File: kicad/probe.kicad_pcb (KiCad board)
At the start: 2 copper layers, 36.2 x 36.2 mm, 5 parts, among them J1 Conn_01x11, J2 Conn_01x11, J3 Conn_01x11, J4 Conn_01x11, U1 QFN44

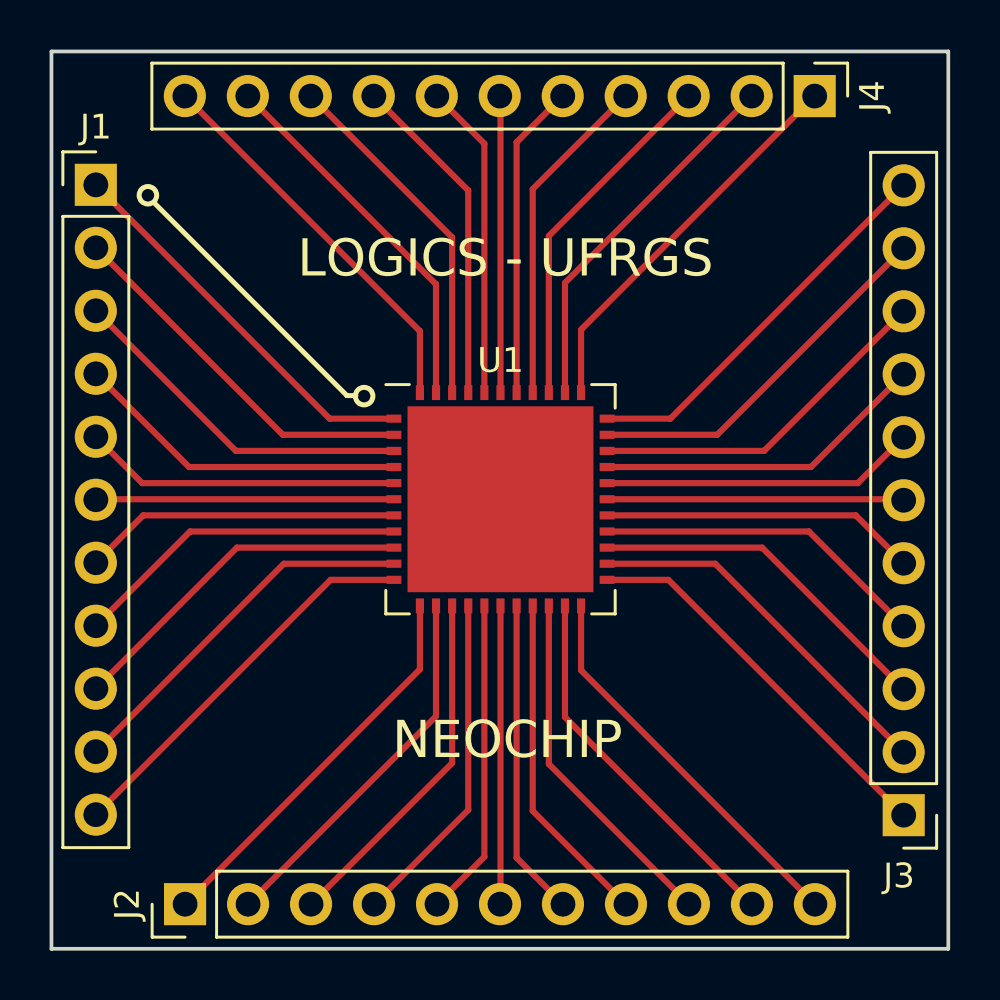
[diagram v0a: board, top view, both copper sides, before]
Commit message: LAYOUT: Modified U1 footprint
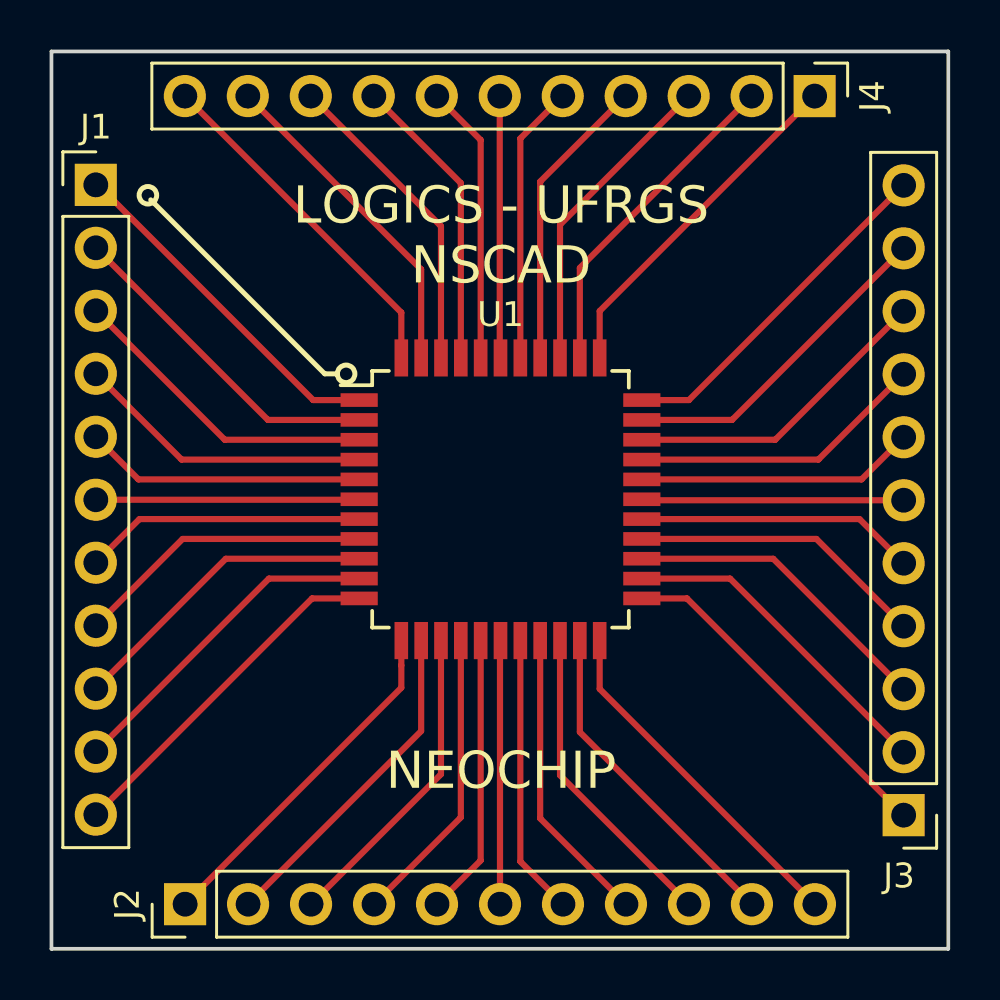
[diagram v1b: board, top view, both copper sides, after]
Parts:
- U1: footprint Housings_DFN_QFN:QFN-44-1EP_9x9mm_Pitch0.65mm -> Housings_QFP:TQFP-44_10x10mm_Pitch0.8mm
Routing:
- net Net-(J4-Pad1): track 15.9 -> 14.2 mm
- net Net-(J4-Pad11): track 15.9 -> 14.2 mm
- net Net-(J2-Pad11): track 15.9 -> 14.2 mm
- net Net-(J2-Pad1): track 16.0 -> 14.2 mm
- net Net-(J1-Pad11): track 15.9 -> 14.2 mm
- net Net-(J1-Pad1): track 15.9 -> 14.2 mm
- net Net-(J3-Pad1): track 15.9 -> 14.2 mm
- net Net-(J3-Pad11): track 15.9 -> 14.1 mm
- net Net-(J4-Pad2): track 15.1 -> 13.4 mm
- net Net-(J4-Pad10): track 15.1 -> 13.5 mm
- net Net-(J2-Pad2): track 15.2 -> 13.5 mm
- net Net-(J2-Pad10): track 15.2 -> 13.5 mm
- net Net-(J1-Pad2): track 15.1 -> 13.5 mm
- net Net-(J1-Pad10): track 15.2 -> 13.5 mm
- net Net-(J3-Pad2): track 15.1 -> 13.5 mm
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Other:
- board text added: "LOGICS - UFRGS NSCAD"
- board text removed: "LOGICS - UFRGS"
